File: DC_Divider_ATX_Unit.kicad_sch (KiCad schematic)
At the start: 5 parts, among them J1 ATX-24, J2 Conn_01x02, J3 Conn_01x02, J4 Conn_01x02, U1 YAAJ_DCDC_StepDown_LM2596

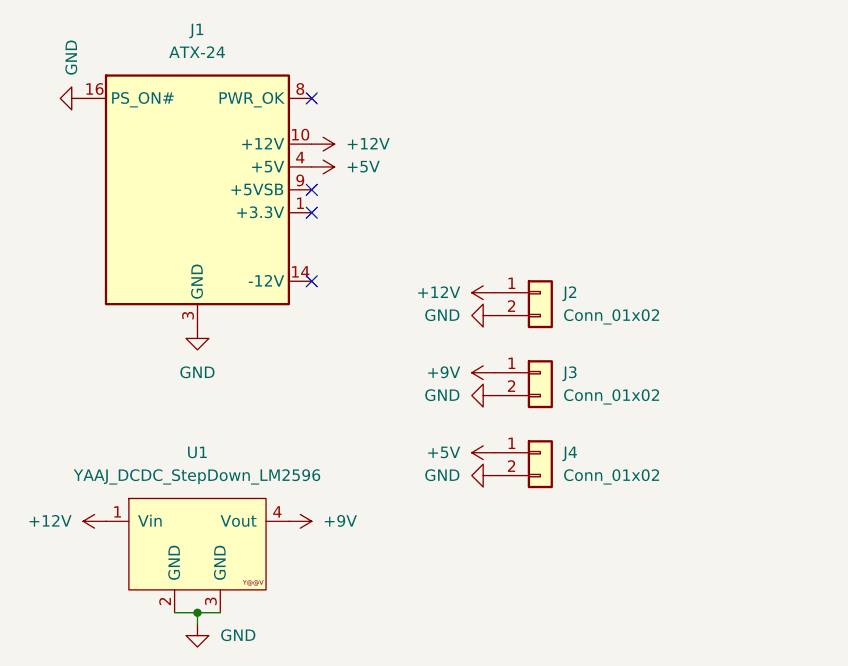
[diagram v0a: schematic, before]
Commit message: Revised PCB design w/ space for fuse holders.
Minival-like blade fuse holders were included in series with each power rail in order to prevent catastrophic damage to the board in a short circuit/overcurrent situation.
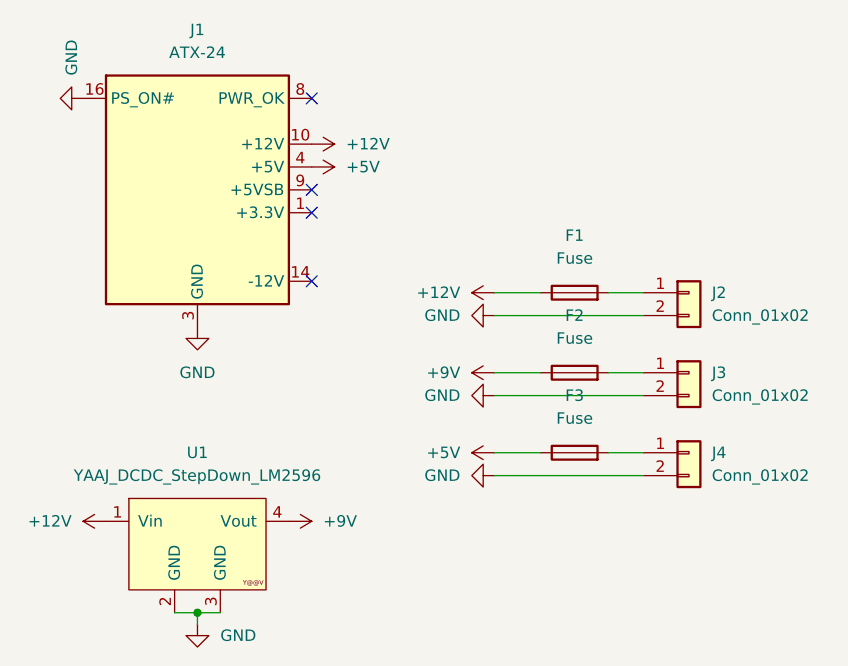
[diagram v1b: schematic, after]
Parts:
- added F1, F2, F3: Fuse, Fuse:Fuseholder_Blade_Mini_Keystone_3568, symbol Device:Fuse
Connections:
- net +12V: now also F1.1; no longer J2.1 (Pin_1)
- net +5V: now also F3.1; no longer J4.1 (Pin_1)
- net +9V: now also F2.1; no longer J3.1 (Pin_1)
- new net: F1.2, J2.1 (Pin_1)
- new net: F3.2, J4.1 (Pin_1)
- new net: F2.2, J3.1 (Pin_1)
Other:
- moved on the sheet: J2, J3, J4
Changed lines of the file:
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@@
   (no_connect (at 127 53.34))
   (no_connect (at 127 73.66))
+  (wire (pts (xy 152.4 92.71) (xy 147.32 92.71))
+    (stroke (width 0) (type default) (color 0 0 0 0))
+  )
+  (wire (pts (xy 163.83 83.82) (xy 160.02 83.82))
+    (stroke (width 0) (type default) (color 0 0 0 0))
+  )
+  (wire (pts (xy 163.83 77.47) (xy 147.32 77.47))
+    (stroke (width 0) (type default) (color 0 0 0 0))
+  )
   (wire (pts (xy 111.76 110.49) (xy 114.3 110.49))
     (stroke (width 0) (type default) (color 0 0 0 0))
   )
+  (wire (pts (xy 163.83 95.25) (xy 147.32 95.25))
+    (stroke (width 0) (type default) (color 0 0 0 0))
+  )
+  (wire (pts (xy 163.83 92.71) (xy 160.02 92.71))
+    (stroke (width 0) (type default) (color 0 0 0 0))
+  )
   (wire (pts (xy 114.3 110.49) (xy 114.3 111.76))
     (stroke (width 0) (type default) (color 0 0 0 0))
   )
+  (wire (pts (xy 152.4 74.93) (xy 147.32 74.93))
+    (stroke (width 0) (type default) (color 0 0 0 0))
+  )
+  (wire (pts (xy 152.4 83.82) (xy 147.32 83.82))
+    (stroke (width 0) (type default) (color 0 0 0 0))
+  )
+  (wire (pts (xy 163.83 86.36) (xy 147.32 86.36))
+    (stroke (width 0) (type default) (color 0 0 0 0))
+  )
+  (wire (pts (xy 163.83 74.93) (xy 160.02 74.93))
+    (stroke (width 0) (type default) (color 0 0 0 0))
+  )
   (wire (pts (xy 116.84 110.49) (xy 114.3 110.49))
     (stroke (width 0) (type default) (color 0 0 0 0))
   )
-  (symbol (lib_id "Connector_Generic:Conn_01x02") (at 152.4 74.93 0) (unit 1)
-    (in_bom yes) (on_board yes) (fields_autoplaced)
-    (property "Reference" "J2" (id 0) (at 154.94 74.9299 0)
-      (effects (font (size 1.27 1.27)) (justify left))
-    )
-    (property "Value" "Conn_01x02" (id 1) (at 154.94 77.4699 0)
-      (effects (font (size 1.27 1.27)) (justify left))
-    )
-    (property "Footprint" "Connector_Phoenix_MSTB:PhoenixContact_MSTBA_2,5_2-G-5,08_1x02_P5.08mm_Horizontal" (id 2) (at 152.4 74.93 0)
-      (effects (font (size 1.27 1.27)) hide)
-    )
-    (property "Datasheet" "~" (id 3) (at 152.4 74.93 0)
+  (symbol (lib_id "Connector_Generic:Conn_01x02") (at 168.91 74.93 0) (unit 1)
+    (in_bom yes) (on_board yes) (fields_autoplaced)
+    (property "Reference" "J2" (id 0) (at 171.45 74.9299 0)
+      (effects (font (size 1.27 1.27)) (justify left))
+    )
+    (property "Value" "Conn_01x02" (id 1) (at 171.45 77.4699 0)
+      (effects (font (size 1.27 1.27)) (justify left))
+    )
+    (property "Footprint" "Connector_Phoenix_MSTB:PhoenixContact_MSTBA_2,5_2-G-5,08_1x02_P5.08mm_Horizontal" (id 2) (at 168.91 74.93 0)
+      (effects (font (size 1.27 1.27)) hide)
+    )
+    (property "Datasheet" "~" (id 3) (at 168.91 74.93 0)
       (effects (font (size 1.27 1.27)) hide)
     )
@@
     )
     (pin "1")
+  )
+  (symbol (lib_id "Device:Fuse") (at 156.21 74.93 90) (unit 1)
+    (in_bom yes) (on_board yes) (fields_autoplaced)
+    (property "Reference" "F1" (id 0) (at 156.21 68.58 90))
+    (property "Value" "Fuse" (id 1) (at 156.21 71.12 90))
+    (property "Footprint" "Fuse:Fuseholder_Blade_Mini_Keystone_3568" (id 2) (at 156.21 76.708 90)
+      (effects (font (size 1.27 1.27)) hide)
+    )
+    (property "Datasheet" "~" (id 3) (at 156.21 74.93 0)
+      (effects (font (size 1.27 1.27)) hide)
+    )
+    (pin "1")
+    (pin "2")
   )
   (symbol (lib_id "yaaj_dcdc_stepdown_lm2596:YAAJ_DCDC_StepDown_LM2596") (at 114.3 102.87 0) (unit 1)
@@
     (pin "1")
   )
-  (symbol (lib_id "Connector_Generic:Conn_01x02") (at 152.4 92.71 0) (unit 1)
-    (in_bom yes) (on_board yes) (fields_autoplaced)
-    (property "Reference" "J4" (id 0) (at 154.94 92.7099 0)
-      (effects (font (size 1.27 1.27)) (justify left))
-    )
-    (property "Value" "Conn_01x02" (id 1) (at 154.94 95.2499 0)
-      (effects (font (size 1.27 1.27)) (justify left))
-    )
-    (property "Footprint" "Connector_Phoenix_MSTB:PhoenixContact_MSTBA_2,5_2-G-5,08_1x02_P5.08mm_Horizontal" (id 2) (at 152.4 92.71 0)
-      (effects (font (size 1.27 1.27)) hide)
-    )
-    (property "Datasheet" "~" (id 3) (at 152.4 92.71 0)
+  (symbol (lib_id "Connector_Generic:Conn_01x02") (at 168.91 92.71 0) (unit 1)
+    (in_bom yes) (on_board yes) (fields_autoplaced)
+    (property "Reference" "J4" (id 0) (at 171.45 92.7099 0)
+      (effects (font (size 1.27 1.27)) (justify left))
+    )
+    (property "Value" "Conn_01x02" (id 1) (at 171.45 95.2499 0)
+      (effects (font (size 1.27 1.27)) (justify left))
+    )
+    (property "Footprint" "Connector_Phoenix_MSTB:PhoenixContact_MSTBA_2,5_2-G-5,08_1x02_P5.08mm_Horizontal" (id 2) (at 168.91 92.71 0)
+      (effects (font (size 1.27 1.27)) hide)
+    )
+    (property "Datasheet" "~" (id 3) (at 168.91 92.71 0)
       (effects (font (size 1.27 1.27)) hide)
     )
@@
     )
     (pin "1")
+  )
+  (symbol (lib_id "Device:Fuse") (at 156.21 83.82 90) (unit 1)
+    (in_bom yes) (on_board yes) (fields_autoplaced)
+    (property "Reference" "F2" (id 0) (at 156.21 77.47 90))
+    (property "Value" "Fuse" (id 1) (at 156.21 80.01 90))
+    (property "Footprint" "Fuse:Fuseholder_Blade_Mini_Keystone_3568" (id 2) (at 156.21 85.598 90)
+      (effects (font (size 1.27 1.27)) hide)
+    )
+    (property "Datasheet" "~" (id 3) (at 156.21 83.82 0)
+      (effects (font (size 1.27 1.27)) hide)
+    )
+    (pin "1")
+    (pin "2")
   )
   (symbol (lib_id "power:+12V") (at 147.32 74.93 90) (unit 1)
@@
     (pin "1")
   )
+  (symbol (lib_id "Device:Fuse") (at 156.21 92.71 90) (unit 1)
+    (in_bom yes) (on_board yes) (fields_autoplaced)
+    (property "Reference" "F3" (id 0) (at 156.21 86.36 90))
+    (property "Value" "Fuse" (id 1) (at 156.21 88.9 90))
+    (property "Footprint" "Fuse:Fuseholder_Blade_Mini_Keystone_3568" (id 2) (at 156.21 94.488 90)
+      (effects (font (size 1.27 1.27)) hide)
+    )
+    (property "Datasheet" "~" (id 3) (at 156.21 92.71 0)
+      (effects (font (size 1.27 1.27)) hide)
+    )
+    (pin "1")
+    (pin "2")
+  )
   (symbol (lib_id "power:+12V") (at 104.14 100.33 90) (unit 1)
     (in_bom yes) (on_board yes) (fields_autoplaced)
@@
     (pin "1")
   )
-  (symbol (lib_id "Connector_Generic:Conn_01x02") (at 152.4 83.82 0) (unit 1)
-    (in_bom yes) (on_board yes) (fields_autoplaced)
-    (property "Reference" "J3" (id 0) (at 154.94 83.8199 0)
-      (effects (font (size 1.27 1.27)) (justify left))
-    )
-    (property "Value" "Conn_01x02" (id 1) (at 154.94 86.3599 0)
-      (effects (font (size 1.27 1.27)) (justify left))
-    )
-    (property "Footprint" "Connector_Phoenix_MSTB:PhoenixContact_MSTBA_2,5_2-G-5,08_1x02_P5.08mm_Horizontal" (id 2) (at 152.4 83.82 0)
-      (effects (font (size 1.27 1.27)) hide)
-    )
-    (property "Datasheet" "~" (id 3) (at 152.4 83.82 0)
+  (symbol (lib_id "Connector_Generic:Conn_01x02") (at 168.91 83.82 0) (unit 1)
+    (in_bom yes) (on_board yes) (fields_autoplaced)
+    (property "Reference" "J3" (id 0) (at 171.45 83.8199 0)
+      (effects (font (size 1.27 1.27)) (justify left))
+    )
+    (property "Value" "Conn_01x02" (id 1) (at 171.45 86.3599 0)
+      (effects (font (size 1.27 1.27)) (justify left))
+    )
+    (property "Footprint" "Connector_Phoenix_MSTB:PhoenixContact_MSTBA_2,5_2-G-5,08_1x02_P5.08mm_Horizontal" (id 2) (at 168.91 83.82 0)
+      (effects (font (size 1.27 1.27)) hide)
+    )
+    (property "Datasheet" "~" (id 3) (at 168.91 83.82 0)
       (effects (font (size 1.27 1.27)) hide)
     )
@@
       (reference "#PWR0114") (unit 1) (value "GND") (footprint "")
     )
+    (path "/319c15be-eae2-460c-8091-84a0ad0a4045"
+      (reference "F1") (unit 1) (value "Fuse") (footprint "Fuse:Fuseholder_Blade_Mini_Keystone_3568")
+    )
+    (path "/7f36da7d-49a4-45e0-9657-51189026110b"
+      (reference "F2") (unit 1) (value "Fuse") (footprint "Fuse:Fuseholder_Blade_Mini_Keystone_3568")
+    )
+    (path "/bd44f37d-e859-4c84-aecf-5ac9120c8f7a"
+      (reference "F3") (unit 1) (value "Fuse") (footprint "Fuse:Fuseholder_Blade_Mini_Keystone_3568")
+    )
     (path "/957be164-cbf0-4d31-80cb-ce5e6ce58b6b"
